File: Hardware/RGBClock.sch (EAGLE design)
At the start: 89 parts, among them IC1 PTH08080W, IC2 LP2985-Digital, IC3 LP2985-Analog, IC4 MCP1824S, IC5 PTH08080W, Q1 MS5V, T1 IRF7205, T2 SI2323, T3 PUMH*, X1 NEB21R, X2 MICRO-SD3

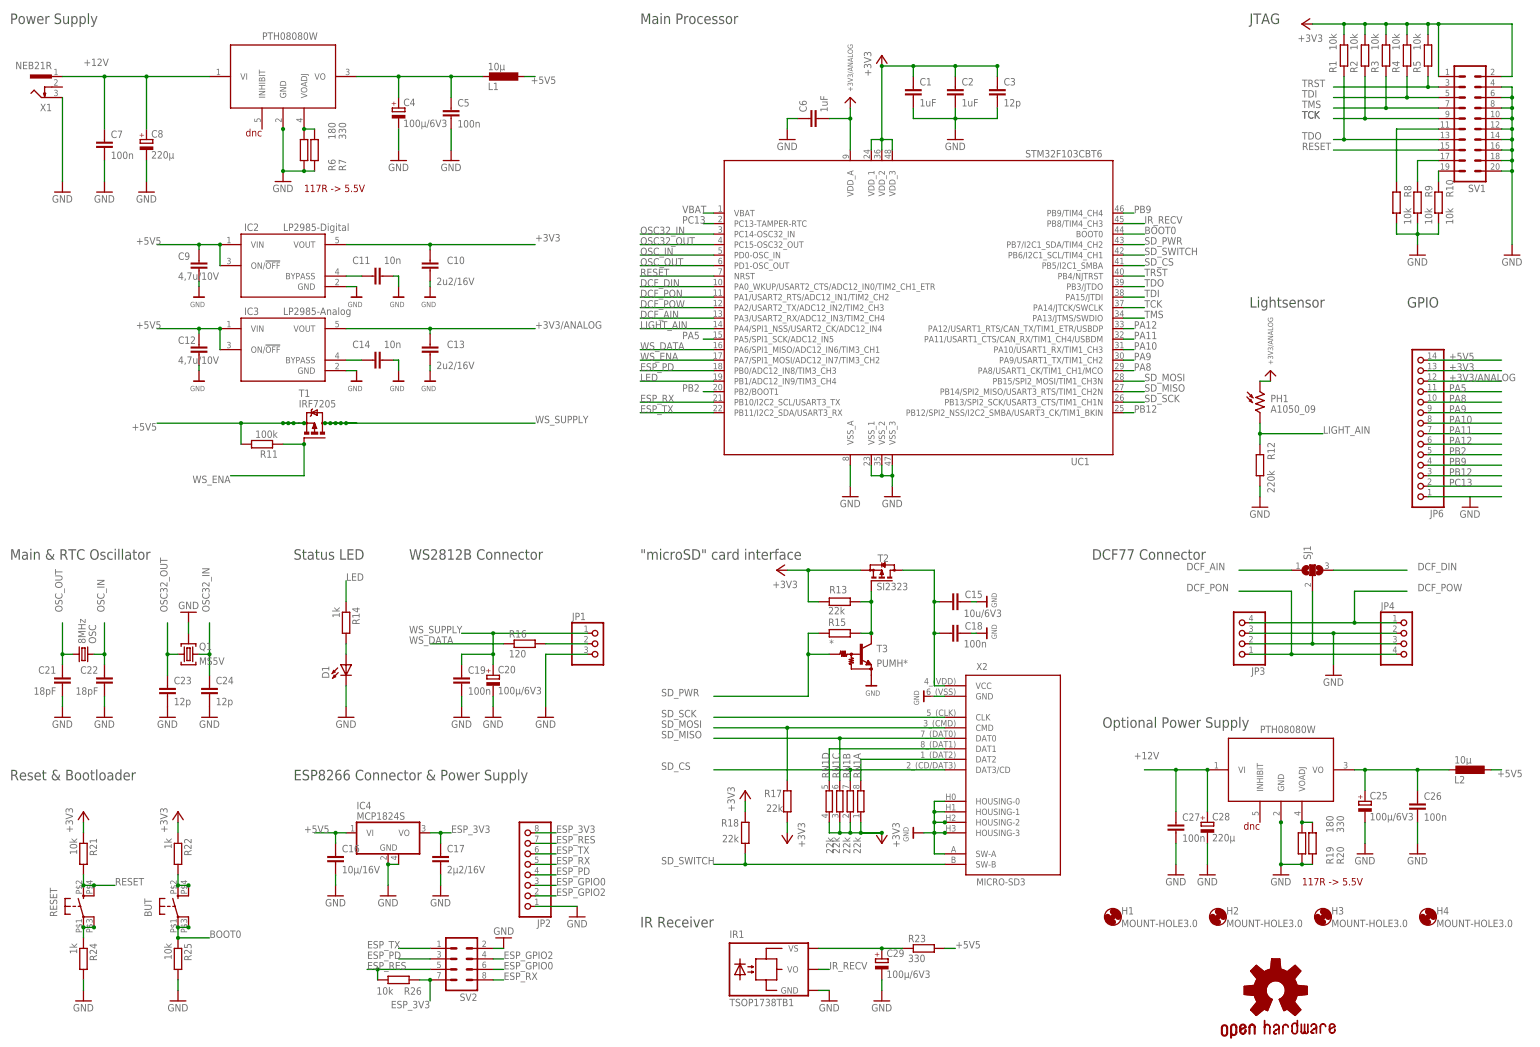
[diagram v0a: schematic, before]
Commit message: worked on board worked on silkscreen -> first version should be ready within a few commits
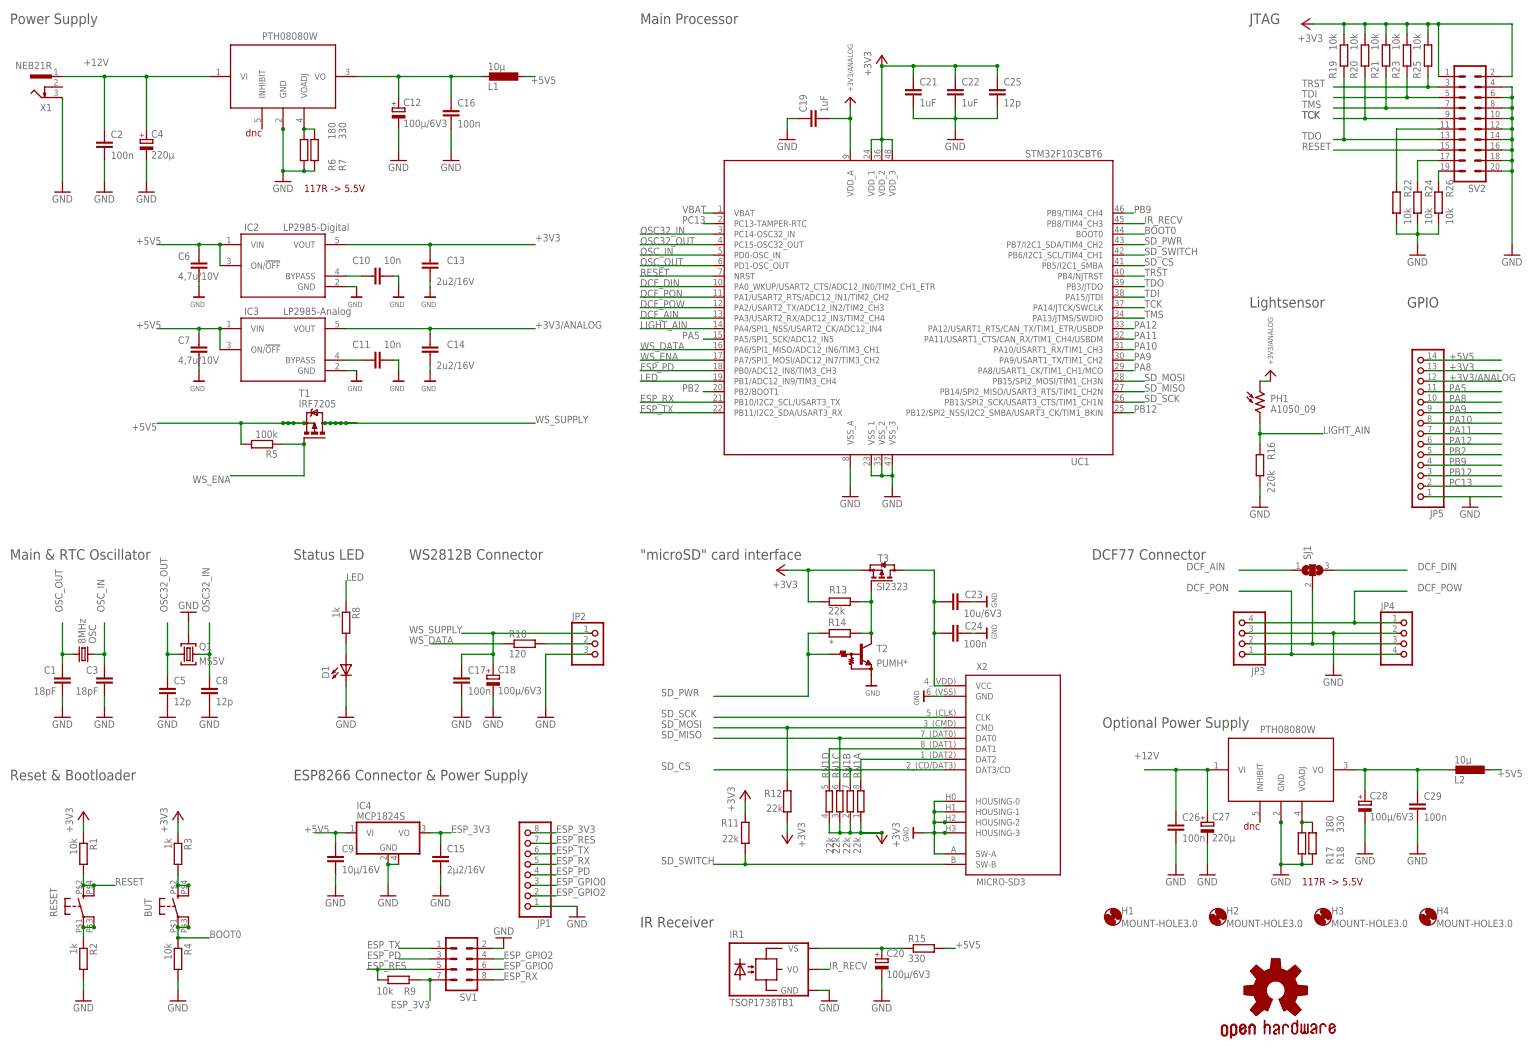
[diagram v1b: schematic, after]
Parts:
- C1: value 1uF -> 18pF; device rcl:C-EUC0603 -> SparkFun:CAP0402
- C10: value 2u2/16V -> 10n
- C12: value 4,7u/10V -> 100µ/6V3; device 00ralf:C0603-DASHES -> rcl:CPOL-EUC
- C14: value 10n -> 2u2/16V
- C15: value 10u/6V3 -> 2µ2/16V; device 00ralf:C0603-DASHES -> rcl:C-EUC0603
- C16: value 10µ/16V -> 100n; device rcl:C-EUC0805 -> rcl:C-EUC0603
- C17: value 2µ2/16V -> 100n
- C18: value 100n -> 100µ/6V3; device 00ralf:C0603-DASHES -> rcl:CPOL-EUC
- C19: value 100n -> 1uF
- C2: value 1uF -> 100n
- C21, C22: value 18pF -> 1uF; device SparkFun:CAP0402 -> rcl:C-EUC0603
- C23: value 12p -> 10u/6V3; device rcl:C-EUC0603 -> 00ralf:C0603-DASHES
- C24: value 12p -> 100n; device rcl:C-EUC0603 -> 00ralf:C0603-DASHES
- C25: value 100µ/6V3 -> 12p; device rcl:CPOL-EUC -> rcl:C-EUC0603
- C27: value 100n -> 220µ; device rcl:C-EUC0603 -> rcl:CPOL-EUE3.5-8
- C28: value 220µ -> 100µ/6V3; device rcl:CPOL-EUE3.5-8 -> rcl:CPOL-EUC
- C29: value 100µ/6V3 -> 100n; device rcl:CPOL-EUC -> rcl:C-EUC0603
- C3: value 12p -> 18pF; device rcl:C-EUC0603 -> SparkFun:CAP0402
- C4: value 100µ/6V3 -> 220µ; device rcl:CPOL-EUC -> rcl:CPOL-EUE3.5-8
- C5: value 100n -> 12p
- C6: value 1uF -> 4,7u/10V; device rcl:C-EUC0603 -> 00ralf:C0603-DASHES
- C7: value 100n -> 4,7u/10V; device rcl:C-EUC0603 -> 00ralf:C0603-DASHES
- C8: value 220µ -> 12p; device rcl:CPOL-EUE3.5-8 -> rcl:C-EUC0603
- C9: value 4,7u/10V -> 10µ/16V; device 00ralf:C0603-DASHES -> rcl:C-EUC0805
- JP1: device pinhead:PINHD-1X3/90 -> pinhead:PINHD-1X8/90
- JP2: device pinhead:PINHD-1X8/90 -> pinhead:PINHD-1X3/90
- R10: value 10k -> 120
- R11: value 100k -> 22k; device rcl:R-EU_R0603 -> 00ralf:R0603-DASHES
- R12: value 220k -> 22k; device rcl:R-EU_R0603 -> 00ralf:R0603-DASHES
- R14: value 1k -> *; device rcl:R-EU_R0603 -> 00ralf:R0603-DASHES
- R15: value * -> 330; device 00ralf:R0603-DASHES -> rcl:R-EU_R0603
- R16: value 120 -> 220k
- R17: value 22k -> 180; device 00ralf:R0603-DASHES -> rcl:R-EU_R0603
- R18: value 22k -> 330; device 00ralf:R0603-DASHES -> rcl:R-EU_R0603
- R19: value 180 -> 10k
- R2, R3, R8: value 10k -> 1k
- R20, R23: value 330 -> 10k
- R22, R24: value 1k -> 10k
- R5: value 10k -> 100k
- SV1: device con-harting-ml:ML20L -> con-lstb:MA04-2
- SV2: device con-lstb:MA04-2 -> con-harting-ml:ML20L
- T2: value SI2323 -> PUMH*; device transistor-fet:SI2323 -> transistor-digital:BCR-SERIES-
- T3: value PUMH* -> SI2323; device transistor-digital:BCR-SERIES- -> transistor-fet:SI2323
- renumbered JP6 to JP5
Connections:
- net +12V: now also C2.1, C26.1, C27.+, C4.+; no longer C27.1, C28.+, C7.1, C8.+
- net +3V3: now also C13.1, C21.1, C22.1, C25.1, R11.2, R12.2, R19.1, R20.1, R23.1, R25.1, SV2.1, SV2.2, T3.S; no longer C1.1, C10.1, C2.1, C3.1, R17.2, R18.2, R2.1, R22.1, R4.1, R5.1, SV1.1, SV1.2, T2.S
- net +3V3/ANALOG: now also C14.1, C19.2; no longer C13.1, C6.2
- net +5V5: now also C6.1, C7.1, R15.2, R5.2; no longer C12.1, C16.1, R11.2, R23.2
- net +6V_EXT: now also C12.+, C16.1; no longer C4.+, C5.1
- net +6V_EXT1: now also C28.+, C29.1; no longer C25.+, C26.1
- net BOOT0: now also R4.1; no longer R25.1
- net ESP_3V3: now also C15.1, JP1.8, R9.2, SV1.7; no longer C17.1, JP2.8, R26.2, SV2.7
- net ESP_GPIO0: now also JP1.3, SV1.6; no longer JP2.3, SV2.6
- net ESP_GPIO2: now also JP1.2, SV1.4; no longer JP2.2, SV2.4
- net ESP_PD: now also JP1.4, SV1.3; no longer JP2.4, SV2.3
- net ESP_RES: now also JP1.7, R9.1, SV1.5; no longer JP2.7, R26.1, SV2.5
- net ESP_RX: now also JP1.5, SV1.8; no longer JP2.5, SV2.8
- net ESP_TX: now also JP1.6, SV1.1; no longer JP2.6, SV2.1
- net GND: now also C12.-, C18.-, C19.1, C25.2, C27.-, C29.2, C6.2, C8.2, JP1.1, JP2.3, R16.1, R17.2, R18.2, R2.2, R22.1, R24.1, R26.1, R4.2, SV1.2, SV2.10, SV2.12, SV2.14, SV2.16, SV2.18, SV2.20, SV2.4, SV2.6, SV2.8, T2.E; no longer C12.2, C18.2, C19.2, C25.-, C27.2, C29.-, C6.1, C8.-, JP1.3, JP2.1, R10.1, R12.1, R19.2, R20.2, R24.2, R25.2, R8.1, R9.1, SV1.10, SV1.12, SV1.14, SV1.16, SV1.18, SV1.20, SV1.4, SV1.6, SV1.8, SV2.2, T3.E
- net LED: now also R8.1; no longer R14.1
- net LIGHT_AIN: now also R16.2; no longer R12.2
- net LP2985_BYPASS: now also C11.1; no longer C14.1
- net LP2985_BYPASS1: now also C10.1; no longer C11.1
- net N$1: now also R3.2; no longer R22.2
- net N$10: now also C20.+, R15.1; no longer C29.+, R23.1
- net N$2: now also R8.2; no longer R14.2
- net N$3: now also JP2.2, R10.2; no longer JP1.2, R16.2
- net N$4: now also R2.1; no longer R24.1
- net N$5: now also R17.1, R18.1; no longer R19.1, R20.1
- net N$6: now also R26.2, SV2.19; no longer R10.2, SV1.19
- net N$8: now also R24.2, SV2.17; no longer R9.2, SV1.17
- net N$9: now also R22.2, SV2.11; no longer R8.2, SV1.11
- net OSC32_IN: now also C8.1; no longer C24.1
- net OSC32_OUT: now also C5.1; no longer C23.1
- net OSC_IN: now also C3.1; no longer C22.1
- net OSC_OUT: now also C1.1; no longer C21.1
- net RESET: now also R1.2, SV2.15; no longer R21.2, SV1.15
- net SDIO_VCC: now also C23.1, C24.1, T3.D; no longer C15.1, C18.1, T2.D
- net SD_MOSI: now also R12.1; no longer R17.1
- net SD_PWR: now also R14.2, T2.B; no longer R15.2, T3.B
- net SD_PWR_INV: now also R14.1, T2.C, T3.G; no longer R15.1, T2.G, T3.C
- net SD_SWITCH: now also R11.1; no longer R18.1
- net TCK: now also R20.2, SV2.9; no longer R2.2, SV1.9
- net TDI: now also R23.2, SV2.5; no longer R4.2, SV1.5
- net TDO: now also R19.2, SV2.13; no longer R1.2, SV1.13
- net TMS: now also R21.2, SV2.7; no longer R3.2, SV1.7
- net TRST: now also R25.2, SV2.3; no longer R5.2, SV1.3
- net WS_DATA: now also R10.1; no longer R16.1
- net WS_ENA: now also R5.1; no longer R11.1
- net WS_SUPPLY: now also C17.1, C18.+, JP2.1; no longer C19.1, C20.+, JP1.1
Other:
- moved on the sheet: C1, C10, C11, C13, C14, C15, C16, C17, C19, C2, C20, C21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

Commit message: minor changes on board and schematic
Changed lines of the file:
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@@
 </segment>
 <segment>
-<wire x1="233.68" y1="370.84" x2="226.06" y2="370.84" width="0.1524" layer="91"/>
 <pinref part="GND29" gate="1" pin="GND"/>
 <pinref part="JP5" gate="A" pin="1"/>
@@
 </segment>
 <segment>
-<wire x1="233.68" y1="403.86" x2="215.9" y2="403.86" width="0.1524" layer="91"/>
+<wire x1="220.98" y1="403.86" x2="215.9" y2="403.86" width="0.1524" layer="91"/>
 <label x="220.98" y="403.86" size="1.778" layer="95"/>
 <pinref part="JP5" gate="A" pin="14"/>
@@
 </segment>
 <segment>
-<wire x1="233.68" y1="398.78" x2="215.9" y2="398.78" width="0.1524" layer="91"/>
+<wire x1="220.98" y1="398.78" x2="215.9" y2="398.78" width="0.1524" layer="91"/>
 <label x="220.98" y="398.78" size="1.778" layer="95"/>
 <pinref part="JP5" gate="A" pin="12"/>
@@
 </segment>
 <segment>
-<wire x1="233.68" y1="378.46" x2="215.9" y2="378.46" width="0.1524" layer="91"/>
+<wire x1="220.98" y1="378.46" x2="215.9" y2="378.46" width="0.1524" layer="91"/>
 <label x="220.98" y="378.46" size="1.778" layer="95"/>
 <pinref part="JP5" gate="A" pin="4"/>
@@
 </segment>
 <segment>
-<wire x1="233.68" y1="383.54" x2="215.9" y2="383.54" width="0.1524" layer="91"/>
+<wire x1="220.98" y1="383.54" x2="215.9" y2="383.54" width="0.1524" layer="91"/>
 <label x="220.98" y="383.54" size="1.778" layer="95"/>
 <pinref part="JP5" gate="A" pin="6"/>
@@
 </segment>
 <segment>
-<wire x1="233.68" y1="381" x2="215.9" y2="381" width="0.1524" layer="91"/>
+<wire x1="220.98" y1="381" x2="215.9" y2="381" width="0.1524" layer="91"/>
 <label x="220.98" y="381" size="1.778" layer="95"/>
 <pinref part="JP5" gate="A" pin="5"/>
@@
 </segment>
 <segment>
-<wire x1="233.68" y1="396.24" x2="215.9" y2="396.24" width="0.1524" layer="91"/>
+<wire x1="220.98" y1="396.24" x2="215.9" y2="396.24" width="0.1524" layer="91"/>
 <label x="220.98" y="396.24" size="1.778" layer="95"/>
 <pinref part="JP5" gate="A" pin="11"/>
@@
 </segment>
 <segment>
-<wire x1="233.68" y1="386.08" x2="215.9" y2="386.08" width="0.1524" layer="91"/>
+<wire x1="220.98" y1="386.08" x2="215.9" y2="386.08" width="0.1524" layer="91"/>
 <label x="220.98" y="386.08" size="1.778" layer="95"/>
 <pinref part="JP5" gate="A" pin="7"/>
@@
 </segment>
 <segment>
-<wire x1="233.68" y1="388.62" x2="215.9" y2="388.62" width="0.1524" layer="91"/>
+<wire x1="223.52" y1="388.62" x2="215.9" y2="388.62" width="0.1524" layer="91"/>
 <label x="220.98" y="388.62" size="1.778" layer="95"/>
 <pinref part="JP5" gate="A" pin="8"/>
@@
 </segment>
 <segment>
-<wire x1="233.68" y1="391.16" x2="215.9" y2="391.16" width="0.1524" layer="91"/>
+<wire x1="220.98" y1="391.16" x2="215.9" y2="391.16" width="0.1524" layer="91"/>
 <label x="220.98" y="391.16" size="1.778" layer="95"/>
 <pinref part="JP5" gate="A" pin="9"/>
@@
 </segment>
 <segment>
-<wire x1="233.68" y1="393.7" x2="215.9" y2="393.7" width="0.1524" layer="91"/>
+<wire x1="220.98" y1="393.7" x2="215.9" y2="393.7" width="0.1524" layer="91"/>
 <label x="220.98" y="393.7" size="1.778" layer="95"/>
 <pinref part="JP5" gate="A" pin="10"/>
@@
 </segment>
 <segment>
-<wire x1="233.68" y1="375.92" x2="215.9" y2="375.92" width="0.1524" layer="91"/>
+<wire x1="220.98" y1="375.92" x2="215.9" y2="375.92" width="0.1524" layer="91"/>
 <label x="220.98" y="375.92" size="1.778" layer="95"/>
 <pinref part="JP5" gate="A" pin="3"/>
@@
 </segment>
 <segment>
-<wire x1="233.68" y1="373.38" x2="215.9" y2="373.38" width="0.1524" layer="91"/>
+<wire x1="220.98" y1="373.38" x2="215.9" y2="373.38" width="0.1524" layer="91"/>
 <label x="220.98" y="373.38" size="1.778" layer="95"/>
 <pinref part="JP5" gate="A" pin="2"/>
@@
 </segment>
 <segment>
-<wire x1="233.68" y1="401.32" x2="215.9" y2="401.32" width="0.1524" layer="91"/>
+<wire x1="220.98" y1="401.32" x2="215.9" y2="401.32" width="0.1524" layer="91"/>
 <label x="220.98" y="401.32" size="1.778" layer="95"/>
 <pinref part="JP5" gate="A" pin="13"/>
